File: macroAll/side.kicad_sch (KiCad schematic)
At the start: 0 parts

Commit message: added circuitry
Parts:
- added D1, D10, D11, D12, D17, D18, D19, D20, D25, D26, D27, D28, D3, D35, D36, D37, D38, D39, D5, D7, D9: D, symbol Device:D
- added H1, H3, H5, H7, H9: MountingHole, symbol Mechanical:MountingHole
- added R1: 806k, symbol Device:R
- added R3: 2M, symbol Device:R
- added SW1, SW10, SW11, SW12, SW17, SW18, SW19, SW20, SW25, SW26, SW27, SW28, SW3, SW35, SW36, SW37, SW38, SW39, SW5, SW7, SW9: SW_Push, symbol Switch:SW_Push
- added TP1: BAT, symbol Connector:TestPoint
- added TP3: GND, symbol Connector:TestPoint
- added U1: XIAO-nRF52840-SMD, modifiedOPL:XIAO-nRF52840-SMD, symbol modifiedOPL:XIAO-nRF52840-SMD
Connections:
- new net: D26.2 (A), SW26.2
- new net: D37.2 (A), SW37.2
- new net: D12.2 (A), SW12.2
- new net: D39.2 (A), SW39.2
- new net: D25.2 (A), SW25.2
- new net: D27.2 (A), SW27.2
- new net: D17.2 (A), SW17.2
- new net: D35.2 (A), SW35.2
- new net: D19.2 (A), SW19.2
- new net: D7.2 (A), SW7.2
- new net: D28.2 (A), SW28.2
- new net: D3.2 (A), SW3.2
- new net: D11.2 (A), SW11.2
- new net: D9.2 (A), SW9.2
- new net: D5.2 (A), SW5.2
- new net: D20.2 (A), SW20.2
- new net: D18.2 (A), SW18.2
- new net: D10.2 (A), SW10.2
- new net: D38.2 (A), SW38.2
- new net: D36.2 (A), SW36.2
- new net: D1.2 (A), SW1.2
- new net BP_PIN: U1.1 (P0.02_A0_D0)
- new net BT_PIN: R1.2, R3.1
- new net COL0: SW1.1, SW17.1, SW25.1, SW9.1, U1.2 (P0.03_A1_D1)
- new net COL1: SW10.1, SW18.1, SW26.1, SW3.1, U1.3 (P0.28_A2_D2)
- new net COL2: SW11.1, SW19.1, SW27.1, SW5.1, U1.4 (P0.29_A3_D3)
- new net COL3: SW12.1, SW20.1, SW28.1, SW7.1, U1.5 (P0.04_A4_D4_SDA)
- new net COL4: SW35.1, SW36.1, SW37.1, SW38.1, SW39.1, U1.6 (P0.05_A5_D5_SCL)
- new net GND: R3.2, TP3.1, U1.13 (GND), U1.16 (GND)
- new net ROW0: D1.1 (K), D3.1 (K), D35.1 (K), D5.1 (K), D7.1 (K), U1.11 (P1.15_D10_MOSI)
- new net ROW1: D10.1 (K), D11.1 (K), D12.1 (K), D36.1 (K), D9.1 (K), U1.10 (P1.14_D9_MISO)
- new net ROW2: D17.1 (K), D18.1 (K), D19.1 (K), D20.1 (K), D37.1 (K), U1.9 (P1.13_D8_SCK)
- new net ROW3: D25.1 (K), D26.1 (K), D27.1 (K), D28.1 (K), D38.1 (K), U1.8 (P1.12_D7_RX)
- new net ROW4: D39.1 (K), U1.7 (P1.11_D6_TX)
- new net VBAT: R1.1, TP1.1, U1.15 (BAT)
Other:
- note added: "Battery Sense"
- note added: "Matrix"
- note added: "Mounting Holes"
- note added: "Test Points"
- note added: "xiao"

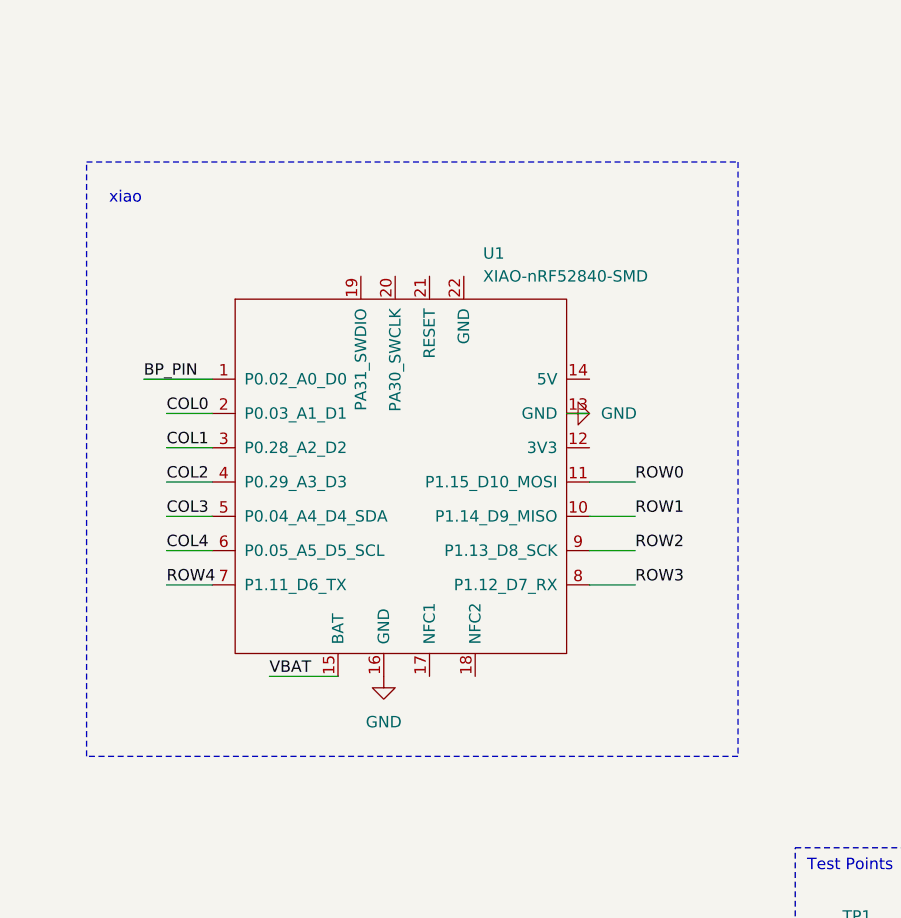
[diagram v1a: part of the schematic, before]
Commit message: Changed circuit board used
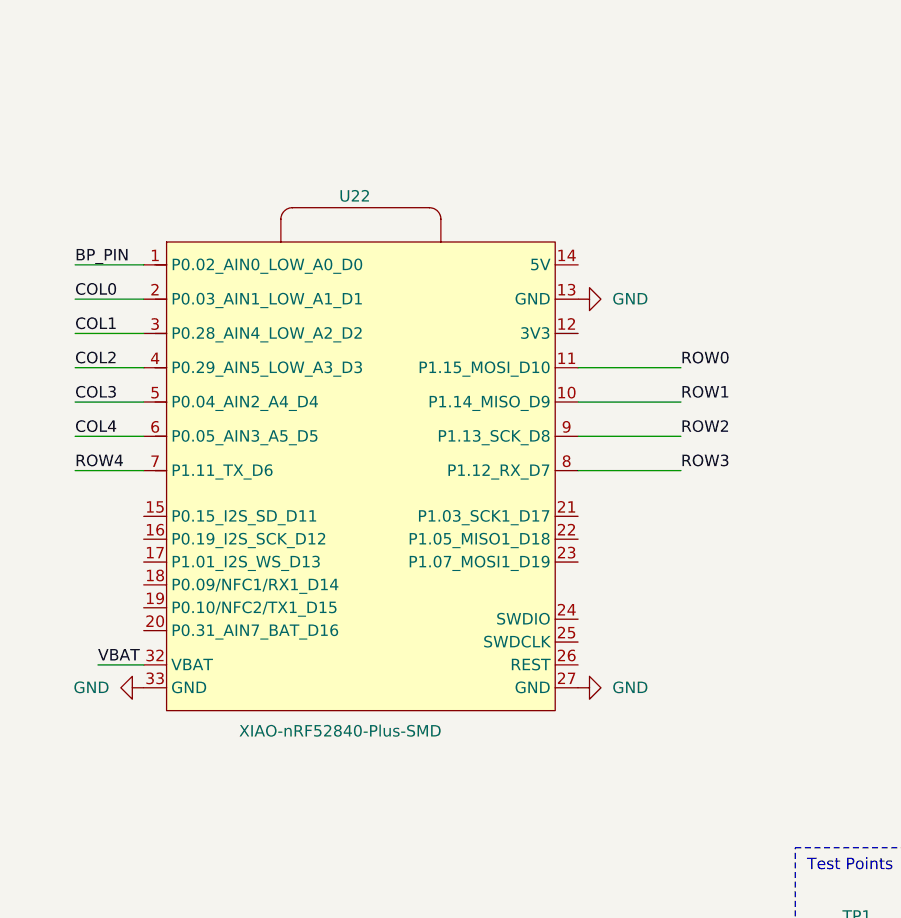
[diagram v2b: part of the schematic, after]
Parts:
- removed U1: XIAO-nRF52840-SMD, modifiedOPL:XIAO-nRF52840-SMD, symbol modifiedOPL:XIAO-nRF52840-SMD
- added U22: XIAO-nRF52840-Plus-SMD, Seeed_Studio_XIAO_Series:XIAO-nRF52840-Plus-SMD, symbol Seeed_Studio_XIAO_Series:XIAO-nRF52840_Plus_SMD
- D1, D10, D11, D12, D17, D18, D19, D20, D25, D26, D27, D28, D3, D35, D36, D37, D38, D39, D5, D7, D9: footprint (none) -> Diode_SMD:D_SOD-123
- R1, R3: footprint (none) -> Resistor_SMD:R_0805_2012Metric
- SW1, SW10, SW11, SW12, SW17, SW18, SW19, SW20, SW25, SW26, SW27, SW28, SW3, SW35, SW36, SW37, SW38, SW39, SW5, SW7, SW9: footprint (none) -> PCM_Switch_Keyboard_Hotswap_Kailh:SW_Hotswap_Kailh_Choc_V1
- TP1, TP3: footprint (none) -> TestPoint:TestPoint_Pad_D2.0mm
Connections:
- net BP_PIN: now also U22.1 (P0.02_AIN0_LOW_A0_D0)
- net COL0: now also U22.2 (P0.03_AIN1_LOW_A1_D1)
- net COL1: now also U22.3 (P0.28_AIN4_LOW_A2_D2)
- net COL2: now also U22.4 (P0.29_AIN5_LOW_A3_D3)
- net COL3: now also U22.5 (P0.04_AIN2_A4_D4)
- net COL4: now also U22.6 (P0.05_AIN3_A5_D5)
- net GND: now also U22.13 (GND), U22.27 (GND), U22.33 (GND)
- net ROW0: now also U22.11 (P1.15_MOSI_D10)
- net ROW1: now also U22.10 (P1.14_MISO_D9)
- net ROW2: now also U22.9 (P1.13_SCK_D8)
- net ROW3: now also U22.8 (P1.12_RX_D7)
- net ROW4: now also U22.7 (P1.11_TX_D6)
- net VBAT: now also U22.32 (VBAT)
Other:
- note removed: "xiao"
- title: (none) -> marcoAll

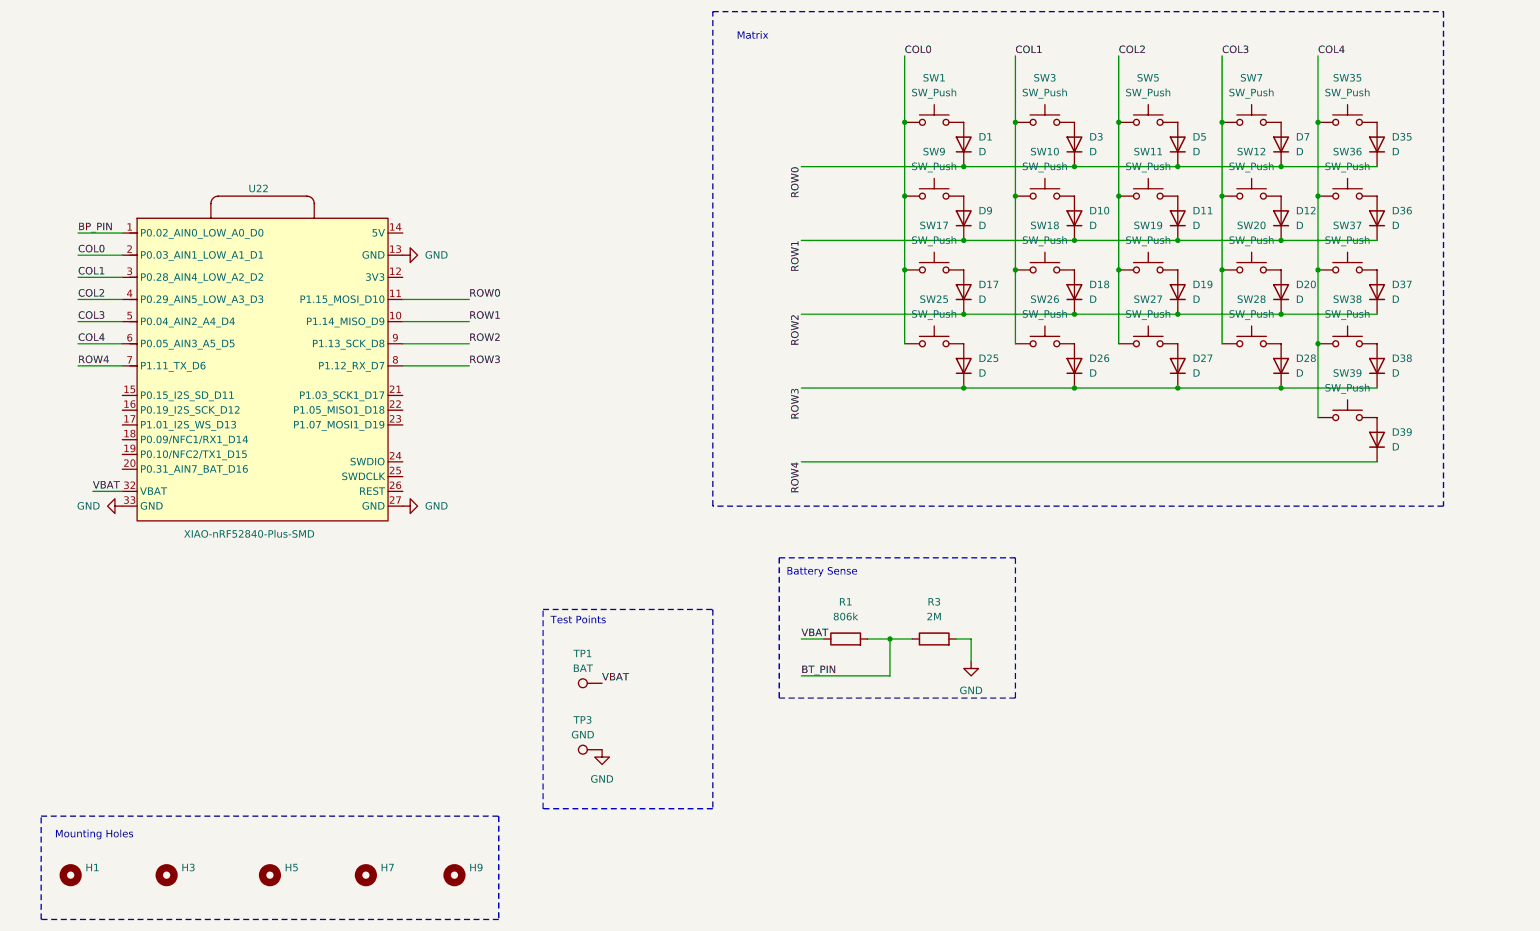
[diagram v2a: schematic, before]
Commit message: fixed footprint
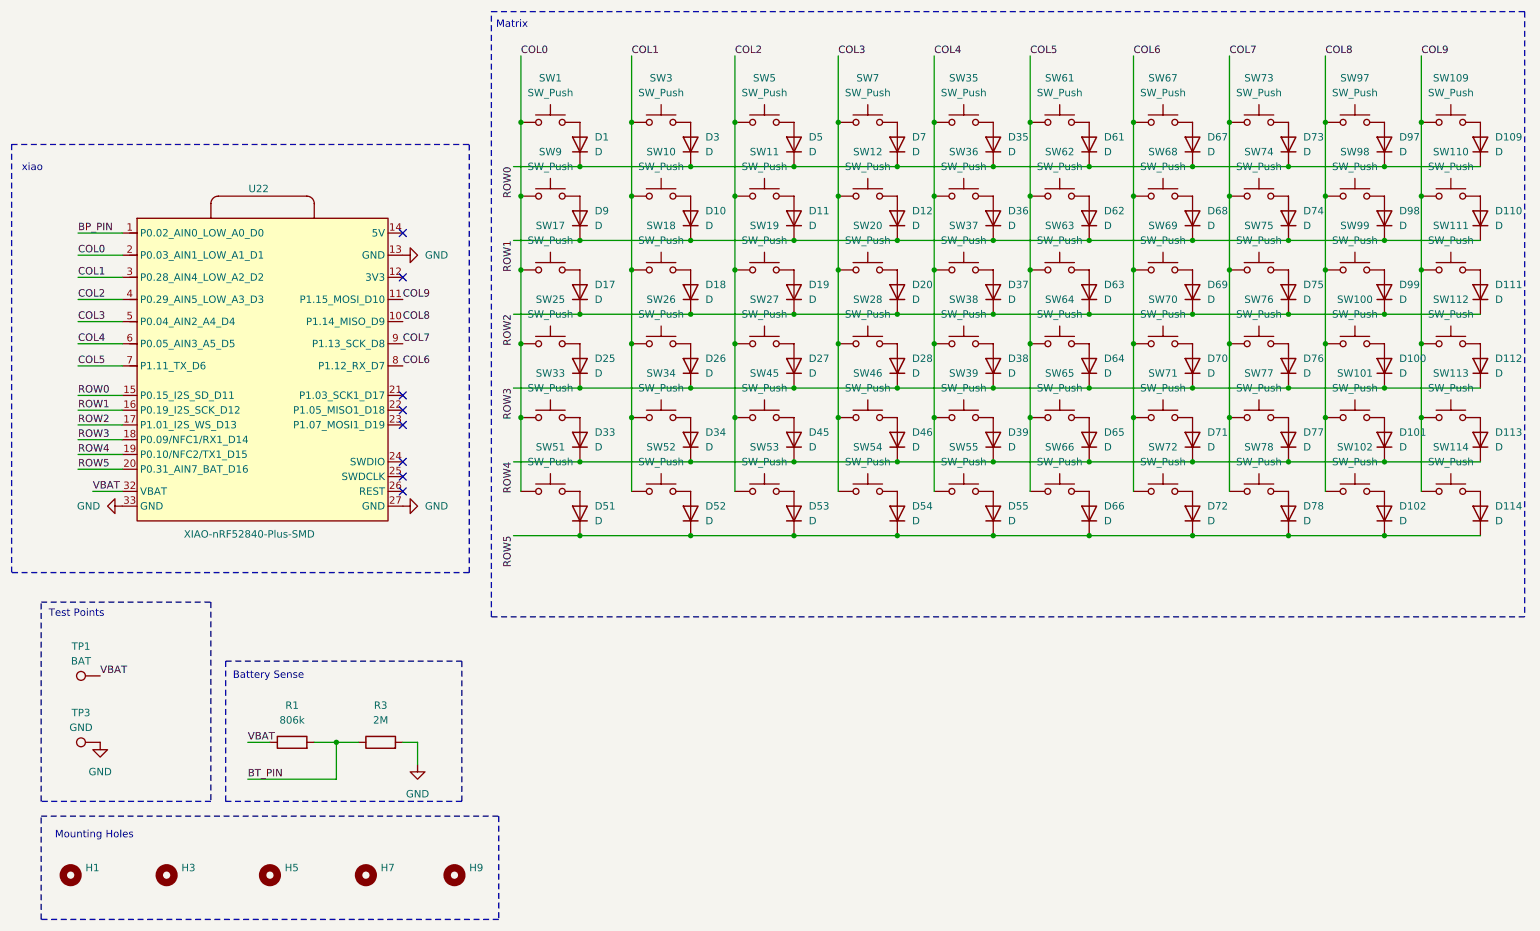
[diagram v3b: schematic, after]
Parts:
- added D100, D101, D102, D109, D110, D111, D112, D113, D114, D33, D34, D45, D46, D51, D52, D53, D54, D55, D61, D62, D63, D64, D65, D66, D67, D68, D69, D70, D71, D72, D73, D74, D75, D76, D77, D78, D97, D98, D99: D, Diode_SMD:D_SOD-123, symbol Device:D
- added SW100, SW101, SW102, SW109, SW110, SW111, SW112, SW113, SW114, SW33, SW34, SW45, SW46, SW51, SW52, SW53, SW54, SW55, SW61, SW62, SW63, SW64, SW65, SW66, SW67, SW68, SW69, SW70, SW71, SW72, SW73, SW74, SW75, SW76, SW77, SW78, SW97, SW98, SW99: SW_Push, PCM_Switch_Keyboard_Hotswap_Kailh:SW_Hotswap_Kailh_Choc_V1, symbol Switch:SW_Push
- H1, H3, H5, H7, H9: footprint (none) -> MountingHole:MountingHole_2.5mm
- U22: footprint Seeed_Studio_XIAO_Series:XIAO-nRF52840-Plus-SMD -> OPL:XIAO-nRF52840-Plus-SMD
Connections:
- net COL0: now also SW33.1, SW51.1
- net COL1: now also SW34.1, SW52.1
- net COL2: now also SW45.1, SW53.1
- net COL3: now also SW46.1, SW54.1
- net COL4: now also SW55.1
- net ROW0: now also U22.15 (P0.15_I2S_SD_D11), D109.1 (K), D61.1 (K), D67.1 (K), D73.1 (K), D97.1 (K); no longer U22.11 (P1.15_MOSI_D10)
- net ROW1: now also U22.16 (P0.19_I2S_SCK_D12), D110.1 (K), D62.1 (K), D68.1 (K), D74.1 (K), D98.1 (K); no longer U22.10 (P1.14_MISO_D9)
- net ROW2: now also U22.17 (P1.01_I2S_WS_D13), D111.1 (K), D63.1 (K), D69.1 (K), D75.1 (K), D99.1 (K); no longer U22.9 (P1.13_SCK_D8)
- net ROW3: now also U22.18 (P0.09/NFC1/RX1_D14), D100.1 (K), D112.1 (K), D64.1 (K), D70.1 (K), D76.1 (K); no longer U22.8 (P1.12_RX_D7)
- net ROW4: now also U22.19 (P0.10/NFC2/TX1_D15), D101.1 (K), D113.1 (K), D33.1 (K), D34.1 (K), D45.1 (K), D46.1 (K), D65.1 (K), D71.1 (K), D77.1 (K); no longer U22.7 (P1.11_TX_D6)
- net ROW5: now reaches U22.20 (P0.31_AIN7_BAT_D16)
- net ROW5: now also D102.1 (K), D114.1 (K), D51.1 (K), D52.1 (K), D53.1 (K), D54.1 (K), D55.1 (K), D66.1 (K), D72.1 (K), D78.1 (K)
- new net: D45.2 (A), SW45.2
- new net: D101.2 (A), SW101.2
- new net: D70.2 (A), SW70.2
- new net: D110.2 (A), SW110.2
- new net: D113.2 (A), SW113.2
- new net: D74.2 (A), SW74.2
- new net: D53.2 (A), SW53.2
- new net: D75.2 (A), SW75.2
- new net: D63.2 (A), SW63.2
- new net: D77.2 (A), SW77.2
- new net: D67.2 (A), SW67.2
- new net: D55.2 (A), SW55.2
- new net: D98.2 (A), SW98.2
- new net: D99.2 (A), SW99.2
- new net: D76.2 (A), SW76.2
- new net: D61.2 (A), SW61.2
- new net: D66.2 (A), SW66.2
- new net: D46.2 (A), SW46.2
- new net: D109.2 (A), SW109.2
- new net: D112.2 (A), SW112.2
- new net: D72.2 (A), SW72.2
- new net: D68.2 (A), SW68.2
- new net: D78.2 (A), SW78.2
- new net: D65.2 (A), SW65.2
- new net: D34.2 (A), SW34.2
- new net: D69.2 (A), SW69.2
- new net: D62.2 (A), SW62.2
- new net: D114.2 (A), SW114.2
- new net: D52.2 (A), SW52.2
- new net: D71.2 (A), SW71.2
- new net: D51.2 (A), SW51.2
- new net: D100.2 (A), SW100.2
- new net: D33.2 (A), SW33.2
- new net: D111.2 (A), SW111.2
- new net: D102.2 (A), SW102.2
- new net: D73.2 (A), SW73.2
- new net: D97.2 (A), SW97.2
- new net: D64.2 (A), SW64.2
- new net: D54.2 (A), SW54.2
- new net COL5: SW61.1, SW62.1, SW63.1, SW64.1, SW65.1, SW66.1, U22.7 (P1.11_TX_D6)
- new net COL6: SW67.1, SW68.1, SW69.1, SW70.1, SW71.1, SW72.1, U22.8 (P1.12_RX_D7)
- new net COL7: SW73.1, SW74.1, SW75.1, SW76.1, SW77.1, SW78.1, U22.9 (P1.13_SCK_D8)
- new net COL8: SW100.1, SW101.1, SW102.1, SW97.1, SW98.1, SW99.1, U22.10 (P1.14_MISO_D9)
- new net COL9: SW109.1, SW110.1, SW111.1, SW112.1, SW113.1, SW114.1, U22.11 (P1.15_MOSI_D10)
- no-connect marks 0 -> 8
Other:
- note added: "xiao"
- moved on the sheet: D1, D10, D11, D12, D17, D18, D19, D20, D25, D26, D27, D28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
